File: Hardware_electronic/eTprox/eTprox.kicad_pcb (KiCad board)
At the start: 2 copper layers, 28.4 x 20.1 mm, 11 parts, among them J1 Conn_01x03, U1 MTCH101

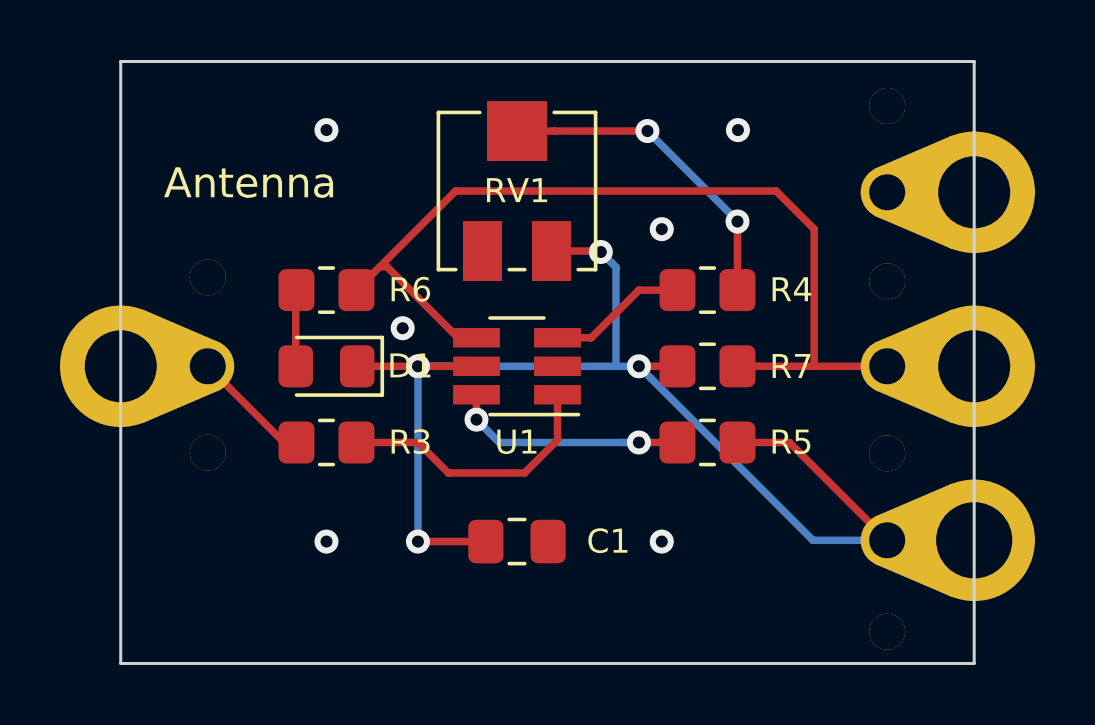
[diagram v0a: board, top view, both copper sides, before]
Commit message: Added JST plug
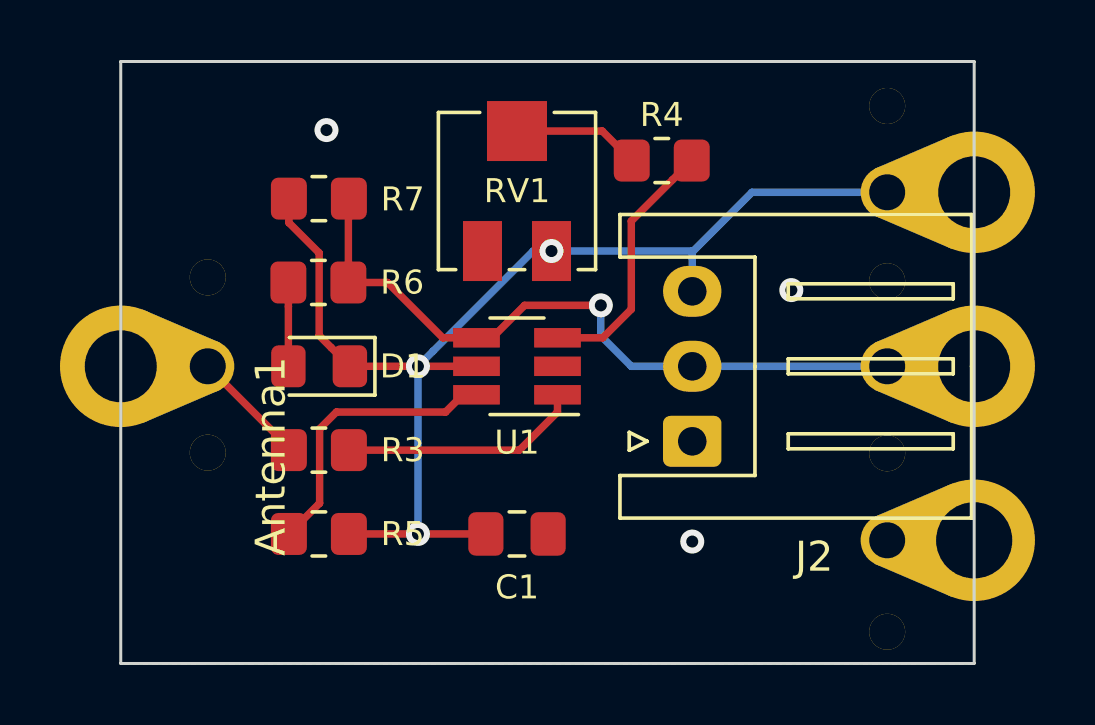
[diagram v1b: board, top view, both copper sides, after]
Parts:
- removed Antenna: Conn_01x01, eTprox:eTprox_Pad_1x01
- added Antenna1: Conn_01x01, eTprox:eTprox_Pad_1x01, F.Cu at (60.8, 68.0)
- added J2: Conn_01x03, Connector_JST:JST_XH_S3B-XH-A_1x03_P2.50mm_Horizontal, F.Cu at (79.8, 70.5)
- RV1: value R_Pot -> 10K
- moved R7 14.1 mm to (67.4, 62.4)
- moved R5 13.3 mm to (67.4, 73.6)
- moved R4 4.58 mm to (78.8, 61.1), turned to 0 degrees
- moved R6 0.37 mm to (67.4, 65.2)
- moved R3 0.36 mm to (67.4, 70.8)
- moved C1 0.25 mm to (74.0, 73.6)
- moved D1 0.25 mm to (67.4, 68.0)
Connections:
- J1 pad 1: GND -> VCC
- J1 pad 3: VCC -> GND
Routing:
- net Net-(R4-Pad1): track 10.9 -> 4.23 mm, vias 2 -> 0
- net Net-(R4-Pad2): track 4.66 -> 8.65 mm
- net GND: track 0.00 -> 2.47 mm, vias 6 -> 3
- net SIG: track 30.9 -> 28.5 mm, vias 0 -> 1
- net Net-(R5-Pad1): track 7.84 -> 9.63 mm, vias 2 -> 0
- net Net-(R3-Pad2): track 9.08 -> 8.05 mm
- net VCC: track 43.2 -> 43.6 mm, vias 4 -> 3

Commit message: Added polarity
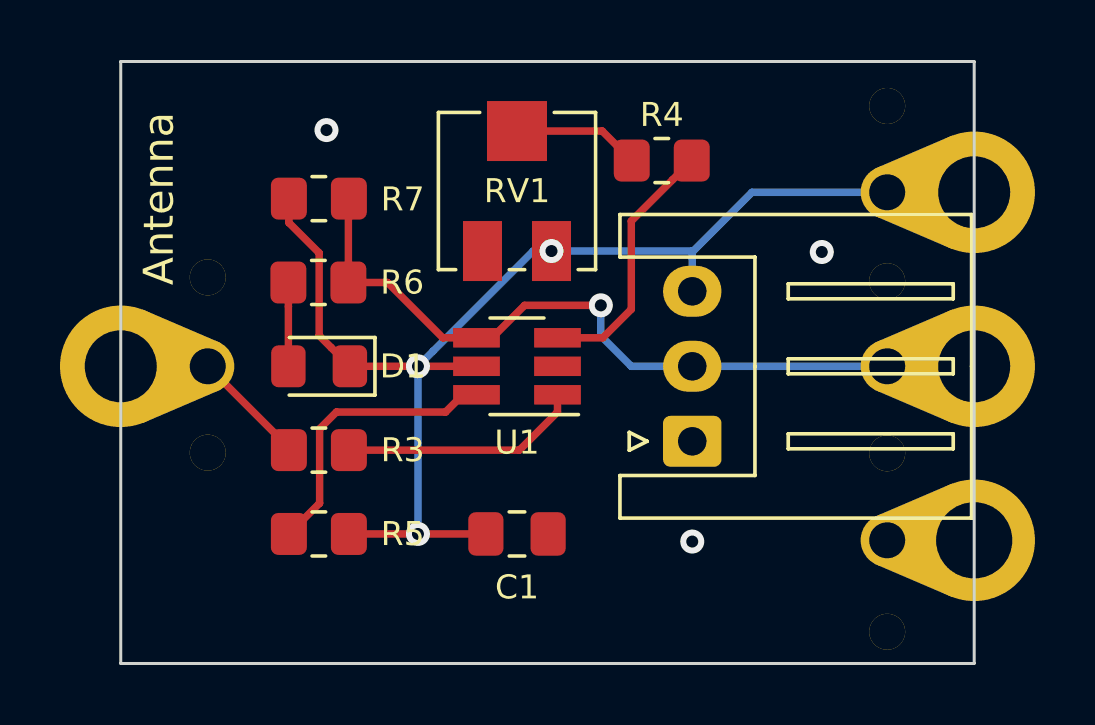
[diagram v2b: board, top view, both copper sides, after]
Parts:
- renumbered Antenna1 to Antenna
